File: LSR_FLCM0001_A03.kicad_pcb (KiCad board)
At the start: 6 copper layers, 30 x 60 mm, 150 parts, among them IC1 FM25L04B-DG, J1 USB_C_Receptacle_USB2.0_16P, J10 SMA_Edge, J2 Conn_01x02_Pin, J3 Conn_01x02_Pin, J4 Conn_ARM_SWD_TagConnect_TC203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, J5 Micro_SD_Card_Det2, J6 2125280200, J7 1771114, J8 Conn_01x05_Pin, J9 SMA_Edge, Q1 AON7296, Q2 AON7296, Q3 AON7296, U1 USBLC6-2SC6, U10 BMP390, U11 MAX-M10S, U12 E22-900MM22S, U2 STM32H742VGH6, U3 W25Q128JVP, U4 TPS62130A, U5 TPS2121RUXR, U6 LSM6DSM, U7 LSM6DS320, U8 LIS2MDL, U9 BMP390, Y1 ABM3B-24.000MHZ

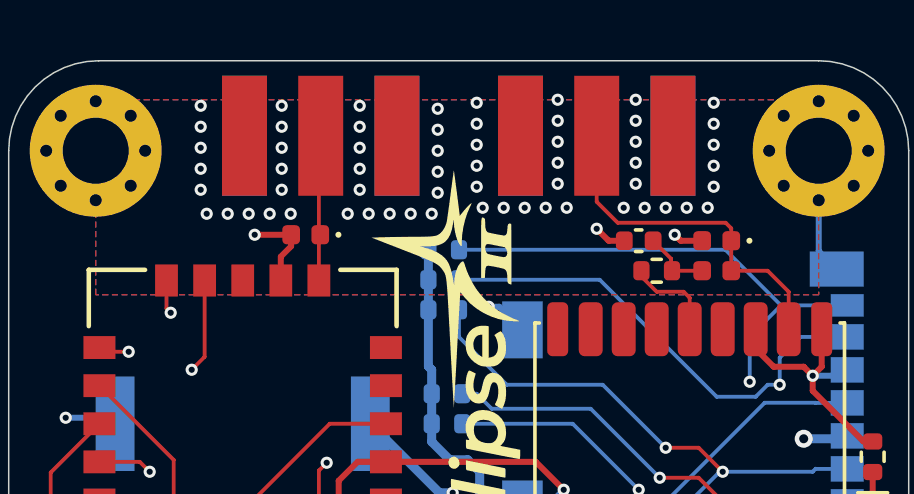
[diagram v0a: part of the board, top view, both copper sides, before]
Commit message: Changed the 3D models and seperated the GPS and the LoRa module antennas
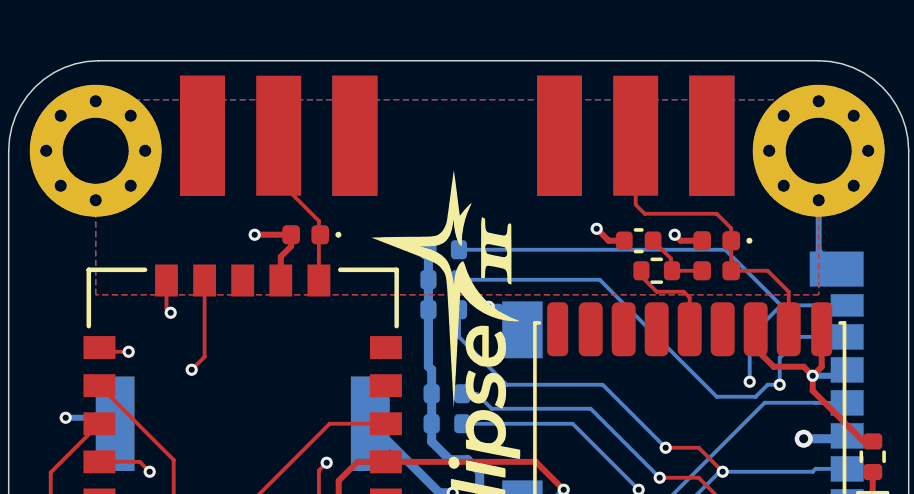
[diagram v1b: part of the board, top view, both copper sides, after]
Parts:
- moved J9 1.40 mm to (144.0, 72.5)
- moved J10 1.30 mm to (155.9, 72.5)
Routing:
- net /Sensors/RF/RF_IN: track 12.0 -> 10.7 mm
- net GND: vias 103 -> 43
